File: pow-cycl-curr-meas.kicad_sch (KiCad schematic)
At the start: 82 parts, among them Q10 2N7002K-T1-E3, Q6 2N7002K-T1-E3, Q7 2N7002K-T1-E3, Q8 2N7002K-T1-E3, Q9 2N7002K-T1-E3, U10 TCA9534, U11 TMCS1100A2-Q1, U12 TMCS1100A2-Q1, U13 TMCS1100A2-Q1, U14 ADS7828, U8 TMCS1100A2-Q1, U9 TMCS1100A2-Q1

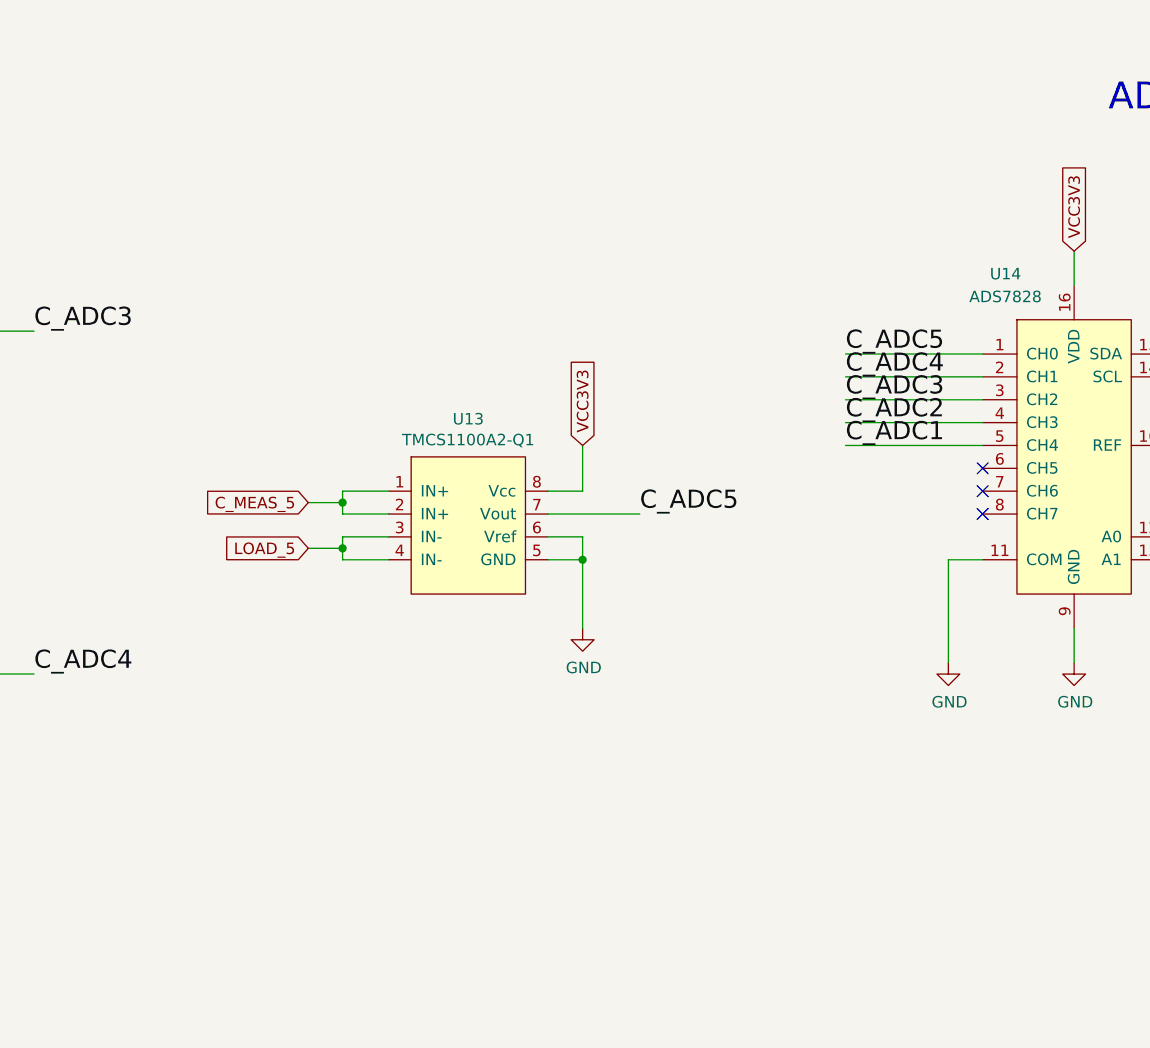
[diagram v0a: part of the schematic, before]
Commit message: Prepared voltage measurement schematic
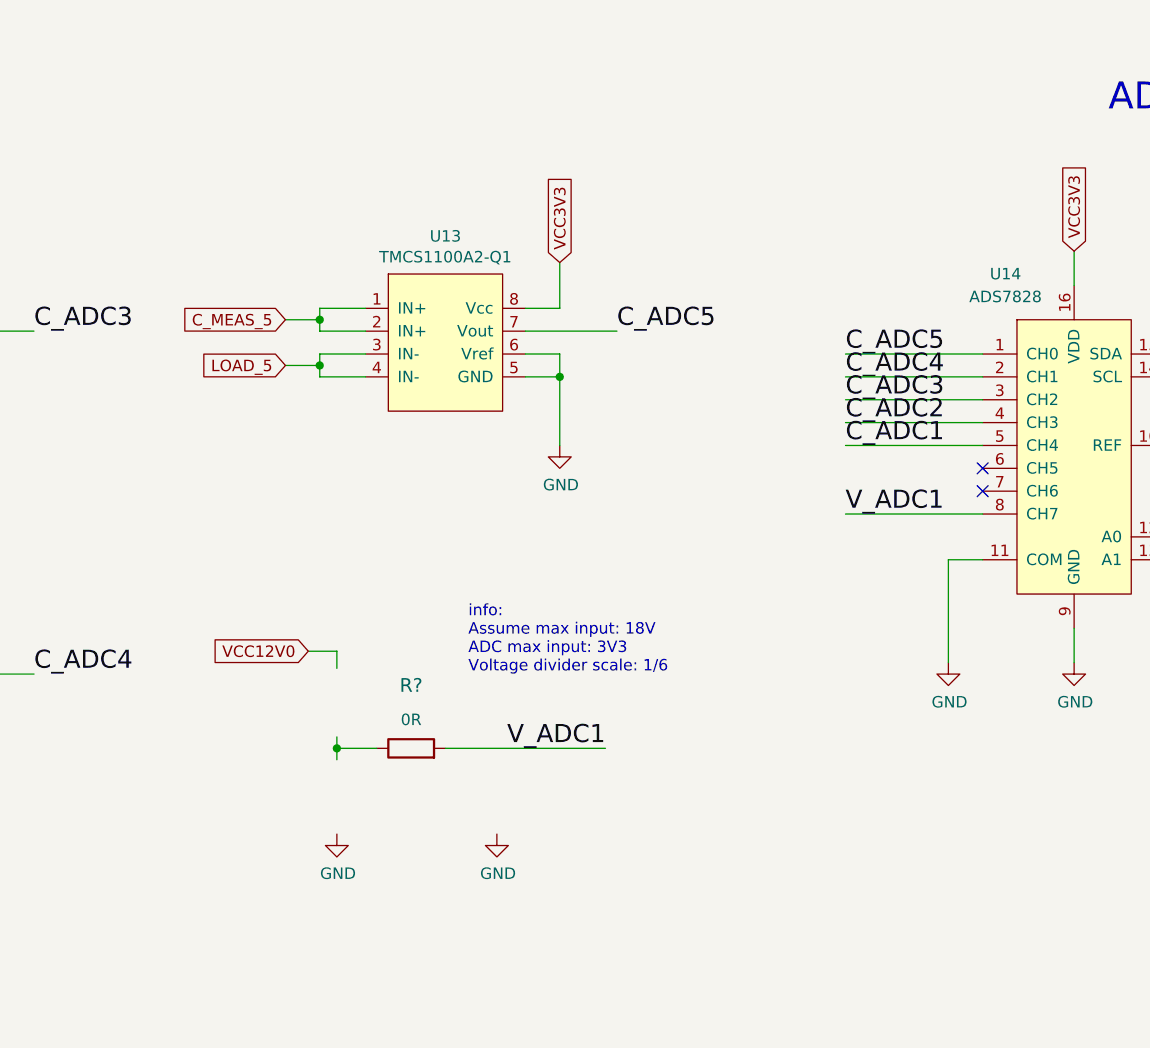
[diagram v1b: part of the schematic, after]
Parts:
- added R?: R_0R_0402, d1600e-psu-breakout-board-footprints:0402-res, symbol d1600e-psu-breakout-board:R_0R_0402
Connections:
- net V_ADC1: now reaches U14.8 (CH7)
- net V_ADC1: now also R?.2
- no-connect marks 6 -> 5
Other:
- note added: "info: Assume max input: 18V ADC max input: 3V3 Voltage divider scale: 1/6"
- moved on the sheet: U13

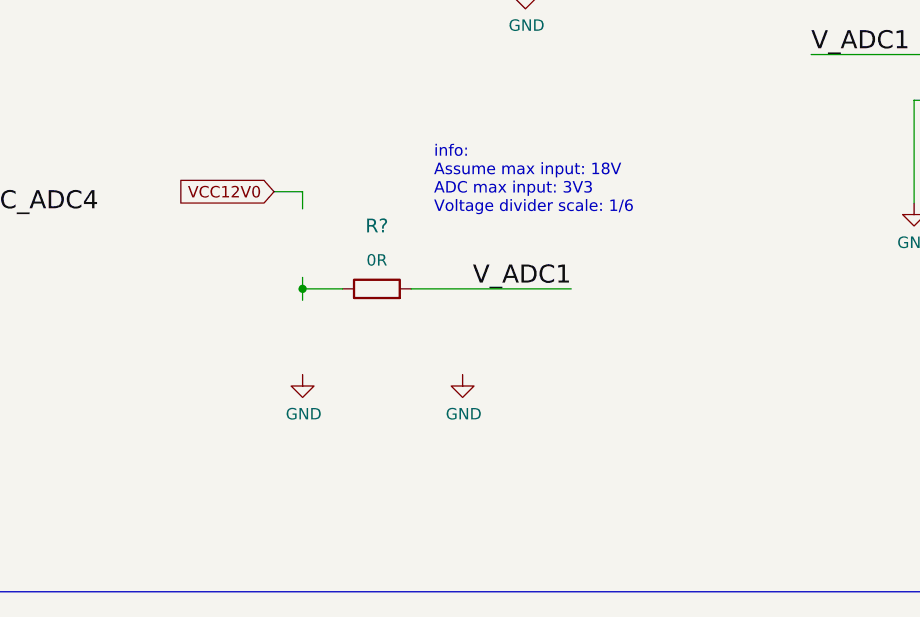
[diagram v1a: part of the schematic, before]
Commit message: Finished voltage measurement schematics
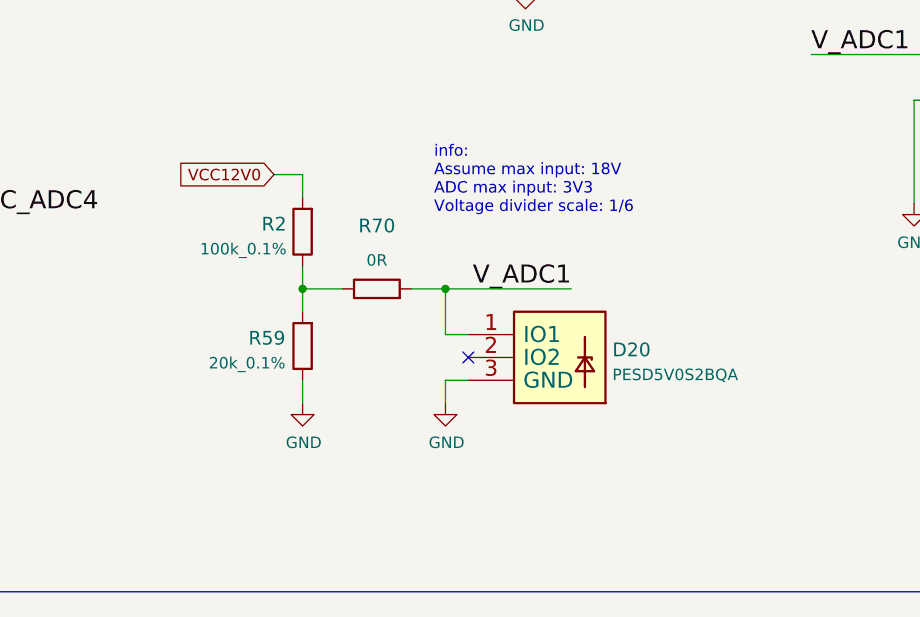
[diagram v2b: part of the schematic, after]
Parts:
- added D20: PESD5V0S2BQA, d1600e-psu-breakout-board-footprints:TPD2E009DRTR, symbol d1600e-psu-breakout-board:PESD5V0S2BQA
- added R2: R_100k_0.1%_0402, antmicro-footprints:0402, symbol antmicroResistors0402:R_100k_0.1%_0402
- added R59: R_20k_0.1%_0402, antmicro-footprints:0402-res, symbol antmicroResistors0402:R_20k_0.1%_0402
- gave numbers to parts that had none: 1
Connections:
- net GND: now also D20.3 (GND), R59.1
- net VCC12V0: now also R2.2
- net V_ADC1: now also D20.1 (IO1)
- net at R70.1: now also R2.1, R59.2
- no-connect marks 5 -> 6
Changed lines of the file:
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@@
   (junction (at 296.545 183.515) (diameter 0) (color 0 0 0 0)
   )
+  (junction (at 198.12 99.695) (diameter 0) (color 0 0 0 0)
+  )
   (junction (at 115.57 90.17) (diameter 0) (color 0 0 0 0)
   )
@@
   )
   (no_connect (at 93.98 195.58))
+  (no_connect (at 200.66 107.315))
   (no_connect (at 93.98 190.5))
   (no_connect (at 254 71.12))
@@
     (stroke (width 0) (type default) (color 0 0 0 0))
   )
-  (wire (pts (xy 212.09 99.695) (xy 194.31 99.695))
+  (wire (pts (xy 212.09 99.695) (xy 198.12 99.695))
     (stroke (width 0) (type default) (color 0 0 0 0))
   )
@@
     (stroke (width 0) (type default) (color 0 0 0 0))
   )
+  (wire (pts (xy 182.245 109.855) (xy 182.245 112.395))
+    (stroke (width 0) (type default) (color 0 0 0 0))
+  )
   (wire (pts (xy 93.98 182.88) (xy 96.52 182.88))
     (stroke (width 0) (type default) (color 0 0 0 0))
@@
     (stroke (width 0) (type default) (color 0 0 0 0))
   )
+  (wire (pts (xy 198.12 104.775) (xy 198.12 99.695))
+    (stroke (width 0) (type default) (color 0 0 0 0))
+  )
   (wire (pts (xy 331.47 63.5) (xy 331.47 59.69))
     (stroke (width 0) (type default) (color 0 0 0 0))
@@
     (stroke (width 0) (type default) (color 0 0 0 0))
   )
+  (wire (pts (xy 200.66 104.775) (xy 198.12 104.775))
+    (stroke (width 0) (type default) (color 0 0 0 0))
+  )
   (wire (pts (xy 337.82 63.5) (xy 337.82 59.69))
     (stroke (width 0) (type default) (color 0 0 0 0))
@@
     (stroke (width 0) (type default) (color 0 0 0 0))
   )
+  (wire (pts (xy 182.245 99.695) (xy 182.245 102.235))
+    (stroke (width 0) (type default) (color 0 0 0 0))
+  )
   (wire (pts (xy 290.195 192.405) (xy 290.195 193.675))
     (stroke (width 0) (type default) (color 0 0 0 0))
@@
     (stroke (width 0) (type default) (color 0 0 0 0))
   )
-  (wire (pts (xy 182.245 88.9) (xy 182.245 90.805))
+  (wire (pts (xy 182.245 86.995) (xy 182.245 89.535))
     (stroke (width 0) (type default) (color 0 0 0 0))
   )
@@
     (stroke (width 0) (type default) (color 0 0 0 0))
   )
-  (wire (pts (xy 182.245 99.695) (xy 182.245 100.965))
-    (stroke (width 0) (type default) (color 0 0 0 0))
-  )
   (wire (pts (xy 35.56 165.1) (xy 35.56 177.8))
     (stroke (width 0) (type default) (color 0 0 0 0))
@@
     (stroke (width 0) (type default) (color 0 0 0 0))
   )
-  (wire (pts (xy 179.07 88.9) (xy 182.245 88.9))
+  (wire (pts (xy 179.07 86.995) (xy 182.245 86.995))
     (stroke (width 0) (type default) (color 0 0 0 0))
   )
@@
     (stroke (width 0) (type default) (color 0 0 0 0))
   )
-  (wire (pts (xy 182.245 98.425) (xy 182.245 99.695))
+  (wire (pts (xy 182.245 97.155) (xy 182.245 99.695))
     (stroke (width 0) (type default) (color 0 0 0 0))
   )
@@
     (stroke (width 0) (type default) (color 0 0 0 0))
   )
+  (wire (pts (xy 198.12 99.695) (xy 194.31 99.695))
+    (stroke (width 0) (type default) (color 0 0 0 0))
+  )
   (wire (pts (xy 220.98 182.245) (xy 220.98 183.515))
     (stroke (width 0) (type default) (color 0 0 0 0))
   )
+  (wire (pts (xy 198.12 109.855) (xy 200.66 109.855))
+    (stroke (width 0) (type default) (color 0 0 0 0))
+  )
   (wire (pts (xy 115.57 52.07) (xy 111.76 52.07))
     (stroke (width 0) (type default) (color 0 0 0 0))
@@
     (stroke (width 0) (type default) (color 0 0 0 0))
   )
+  (wire (pts (xy 198.12 112.395) (xy 198.12 109.855))
+    (stroke (width 0) (type default) (color 0 0 0 0))
+  )
   (wire (pts (xy 120.65 50.8) (xy 115.57 50.8))
     (stroke (width 0) (type default) (color 0 0 0 0))
@@
     (effects (font (size 2.0066 2.0066)) (justify left bottom))
   )
-  (global_label "VCC12V0" (shape input) (at 179.07 88.9 180) (fields_autoplaced)
+  (global_label "VCC12V0" (shape input) (at 179.07 86.995 180) (fields_autoplaced)
     (effects (font (size 1.27 1.27)) (justify right))
-    (property "Intersheet References" "${INTERSHEET_REFS}" (id 0) (at 168.4001 88.8206 0)
+    (property "Intersheet References" "${INTERSHEET_REFS}" (id 0) (at 168.4001 86.9156 0)
       (effects (font (size 1.27 1.27)) (justify right) hide)
     )
@@
   (symbol (lib_id "d1600e-psu-breakout-board:R_0R_0402") (at 190.5 99.695 0) (unit 1)
     (in_bom yes) (on_board yes) (fields_autoplaced)
-    (property "Reference" "R?" (id 0) (at 190.5 92.71 0)
+    (property "Reference" "R70" (id 0) (at 190.5 92.71 0)
       (effects (font (size 1.524 1.524)))
     )
@@
     (pin "5")
   )
+  (symbol (lib_id "antmicroResistors0402:R_100k_0.1%_0402") (at 182.245 93.345 90) (unit 1)
+    (in_bom yes) (on_board yes) (fields_autoplaced)
+    (property "Reference" "R2" (id 0) (at 180.4671 92.5104 90)
+      (effects (font (size 1.524 1.524)) (justify left))
+    )
+    (property "Value" "R_100k_0.1%_0402" (id 1) (at 187.325 93.345 0)
+      (effects (font (size 1.524 1.524)) hide)
+    )
+    (property "Footprint" "antmicro-footprints:0402" (id 2) (at 177.165 88.265 0)
+      (effects (font (size 1.524 1.524)) (justify left) hide)
+    )
+    (property "Datasheet" "https://www.mouser.pl/datasheet/2/447/PYu_RC_Group_51_RoHS_L_11-1984063.pdf" (id 3) (at 189.865 93.345 0)
+      (effects (font (size 1.27 1.27)) hide)
+    )
+    (property "Manufacturer" "Yageo" (id 4) (at 172.085 88.265 0)
+      (effects (font (size 1.524 1.524)) (justify left) hide)
+    )
+    (property "MPN" "RC0402BR-07100KL" (id 5) (at 174.625 88.265 0)
+      (effects (font (size 1.524 1.524)) (justify left) hide)
+    )
+    (property "Val" "100k_0.1%" (id 6) (at 180.4671 95.2755 90)
+      (effects (font (size 1.27 1.27)) (justify left))
+    )
+    (pin "1")
+    (pin "2")
+  )
   (symbol (lib_id "antmicroTransistorsFETsMOSFETsSingle:SI7613DN-T1-GE3") (at 160.655 151.13 270) (mirror x) (unit 1)
     (in_bom yes) (on_board yes) (fields_autoplaced)
@@
     (pin "2")
   )
-  (symbol (lib_id "d1600e-psu-breakout-board:GND") (at 182.245 109.22 0) (unit 1)
+  (symbol (lib_id "d1600e-psu-breakout-board:GND") (at 182.245 112.395 0) (unit 1)
     (in_bom yes) (on_board yes)
-    (property "Reference" "#PWR?" (id 0) (at 182.245 115.57 0)
+    (property "Reference" "#PWR011" (id 0) (at 182.245 118.745 0)
       (effects (font (size 1.27 1.27)) hide)
     )
-    (property "Value" "GND" (id 1) (at 182.372 113.6142 0))
-    (property "Footprint" "d1600e-psu-breakout-board-footprints:" (id 2) (at 182.245 109.22 0)
+    (property "Value" "GND" (id 1) (at 182.372 116.7892 0))
+    (property "Footprint" "d1600e-psu-breakout-board-footprints:" (id 2) (at 182.245 112.395 0)
       (effects (font (size 1.27 1.27)) hide)
     )
-    (property "Datasheet" "" (id 3) (at 182.245 109.22 0)
+    (property "Datasheet" "" (id 3) (at 182.245 112.395 0)
       (effects (font (size 1.27 1.27)) hide)
     )
@@
     (pin "5")
   )
-  (symbol (lib_id "d1600e-psu-breakout-board:GND") (at 200.025 109.22 0) (unit 1)
+  (symbol (lib_id "d1600e-psu-breakout-board:GND") (at 198.12 112.395 0) (unit 1)
     (in_bom yes) (on_board yes)
-    (property "Reference" "#PWR?" (id 0) (at 200.025 115.57 0)
+    (property "Reference" "#PWR016" (id 0) (at 198.12 118.745 0)
       (effects (font (size 1.27 1.27)) hide)
     )
-    (property "Value" "GND" (id 1) (at 200.152 113.6142 0))
-    (property "Footprint" "d1600e-psu-breakout-board-footprints:" (id 2) (at 200.025 109.22 0)
+    (property "Value" "GND" (id 1) (at 198.247 116.7892 0))
+    (property "Footprint" "d1600e-psu-breakout-board-footprints:" (id 2) (at 198.12 112.395 0)
       (effects (font (size 1.27 1.27)) hide)
     )
-    (property "Datasheet" "" (id 3) (at 200.025 109.22 0)
+    (property "Datasheet" "" (id 3) (at 198.12 112.395 0)
       (effects (font (size 1.27 1.27)) hide)
     )
@@
     (pin "5")
   )
+  (symbol (lib_id "d1600e-psu-breakout-board:PESD5V0S2BQA") (at 205.74 104.775 0) (unit 1)
+    (in_bom yes) (on_board yes) (fields_autoplaced)
+    (property "Reference" "D20" (id 0) (at 216.662 106.4804 0)
+      (effects (font (size 1.524 1.524)) (justify left))
+    )
+    (property "Value" "PESD5V0S2BQA" (id 1) (at 198.12 120.015 90)
+      (effects (font (size 1.524 1.524)) (justify left bottom) hide)
+    )
+    (property "Footprint" "d1600e-psu-breakout-board-footprints:TPD2E009DRTR" (id 2) (at 207.01 99.695 0)
+      (effects (font (size 1.524 1.524)) hide)
+    )
+    (property "Datasheet" "" (id 3) (at 205.74 104.775 0)
+      (effects (font (size 1.524 1.524)) hide)
+    )
+    (property "MPN" "PESD5V0S2BQA" (id 4) (at 216.662 109.2455 0)
+      (effects (font (size 1.27 1.27)) (justify left))
+    )
+    (property "Manufacturer" "Nexperia" (id 5) (at 207.01 116.205 0)
+      (effects (font (size 1.27 1.27)) (justify left) hide)
+    )
+    (pin "1")
+    (pin "2")
+    (pin "3")
+  )
+  (symbol (lib_id "antmicroResistors0402:R_20k_0.1%_0402") (at 182.245 106.045 90) (unit 1)
+    (in_bom yes) (on_board yes)
+    (property "Reference" "R59" (id 0) (at 180.34 105.1849 90)
+      (effects (font (size 1.524 1.524)) (justify left))
+    )
+    (property "Value" "R_20k_0.1%_0402" (id 1) (at 187.325 106.045 0)
+      (effects (font (size 1.524 1.524)) hide)
+    )
+    (property "Footprint" "antmicro-footprints:0402-res" (id 2) (at 177.165 100.965 0)
+      (effects (font (size 1.524 1.524)) (justify left) hide)
+    )
+    (property "Datasheet" "https://www.mouser.pl/datasheet/2/447/PYu_RC_Group_51_RoHS_L_11-1984063.pdf" (id 3) (at 189.865 106.045 0)
+      (effects (font (size 1.27 1.27)) hide)
+    )
+    (property "Manufacturer" "Yageo" (id 4) (at 172.085 100.965 0)
+      (effects (font (size 1.524 1.524)) (justify left) hide)
+    )
+    (property "MPN" "RC0402BR-0720KL" (id 5) (at 174.625 100.965 0)
+      (effects (font (size 1.524 1.524)) (justify left) hide)
+    )
+    (property "Val" "20k_0.1%" (id 6) (at 180.34 107.95 90)
+      (effects (font (size 1.27 1.27)) (justify left))
+    )
+    (pin "1")
+    (pin "2")
+  )
   (symbol (lib_id "d1600e-psu-breakout-board:GND") (at 130.175 259.715 0) (unit 1)

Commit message: Implemented voltage measurement on PCB
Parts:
- R2: footprint antmicro-footprints:0402 -> antmicro-footprints:0402-res
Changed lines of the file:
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@@
       (effects (font (size 1.524 1.524)) hide)
     )
-    (property "Footprint" "antmicro-footprints:0402" (id 2) (at 177.165 88.265 0)
+    (property "Footprint" "antmicro-footprints:0402-res" (id 2) (at 177.165 88.265 0)
       (effects (font (size 1.524 1.524)) (justify left) hide)
     )
